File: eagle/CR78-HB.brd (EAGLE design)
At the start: 100 x 80 mm, 34 parts, among them Q1 2N3904, Q2 2N3904, Q3 2N3904, X1 22-23-2021

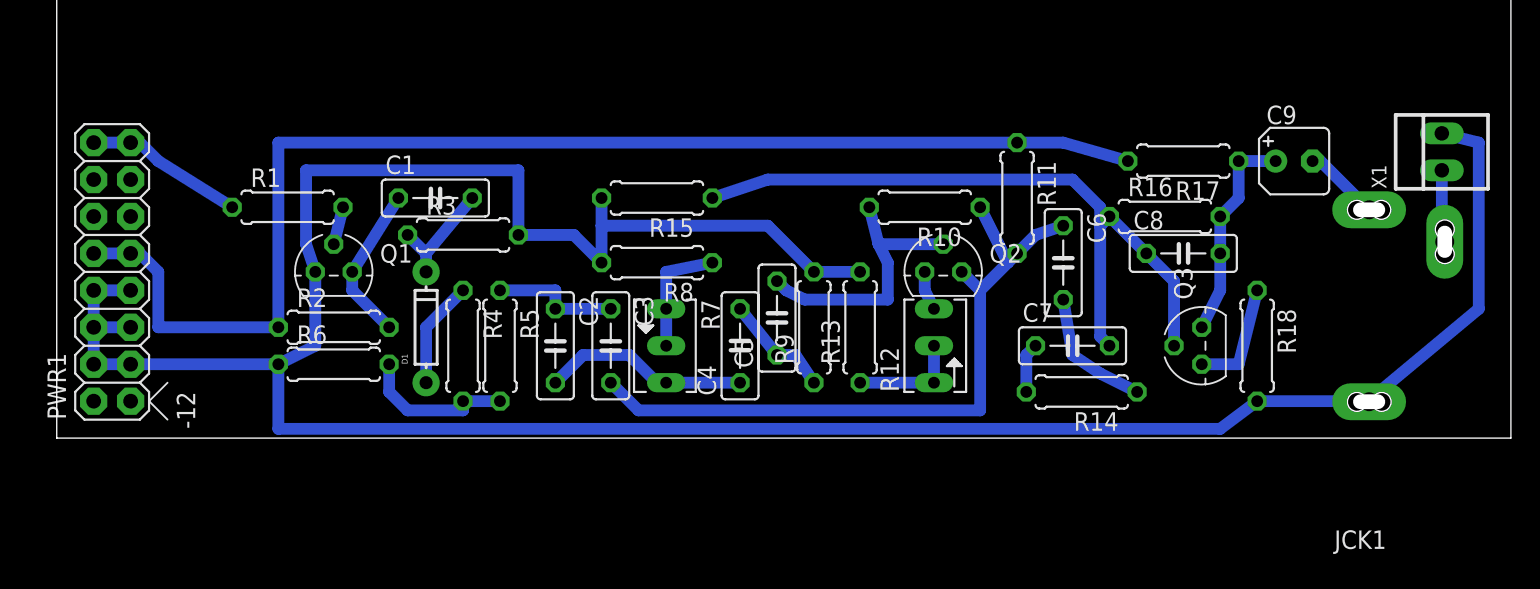
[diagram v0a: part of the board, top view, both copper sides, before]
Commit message: minimized routing
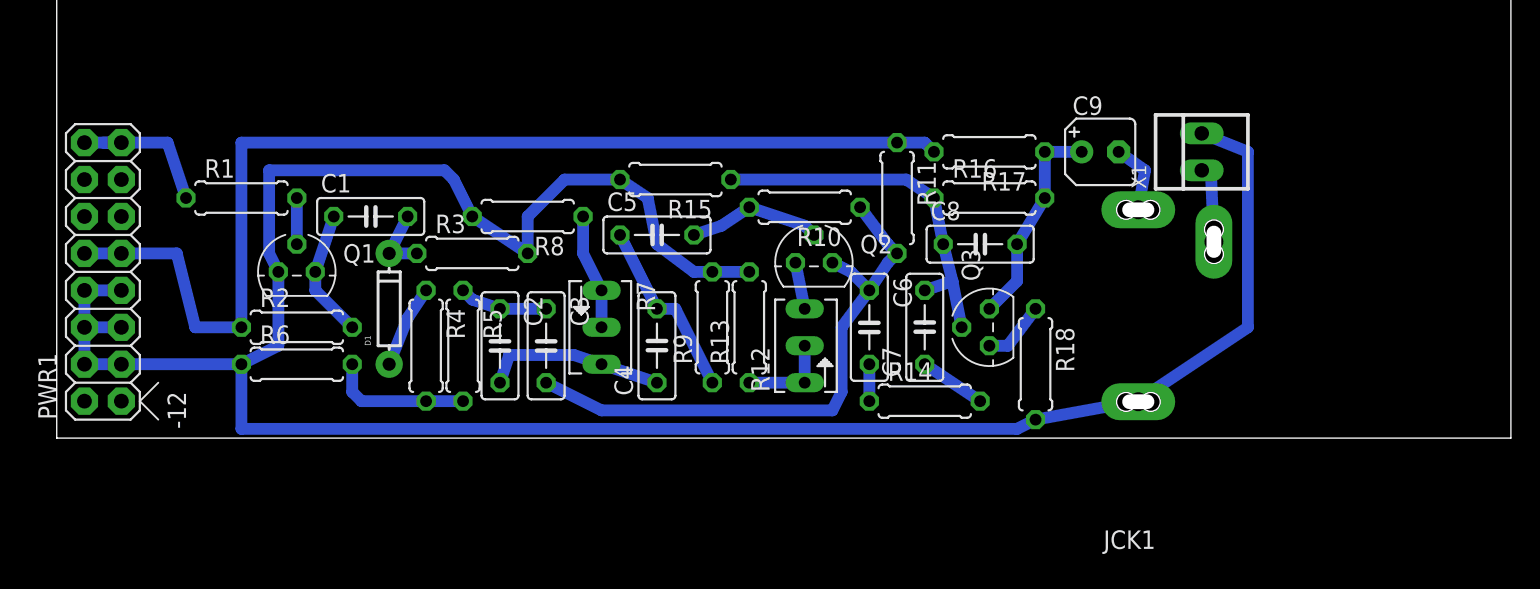
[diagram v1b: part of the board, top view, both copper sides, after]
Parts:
- moved X1 16.5 mm to (78.7, 19.7)
- moved JCK1 15.9 mm to (79.4, 0.00)
- moved R18 15.3 mm to (67.3, 5.08)
- moved Q3 14.7 mm to (64.1, 7.62)
- moved C6 14.1 mm to (55.9, 7.62)
- moved C8 14.0 mm to (63.5, 13.3)
- moved C9 13.4 mm to (71.8, 19.7)
- moved R17 13.4 mm to (64.1, 19.7)
- moved R16 12.1 mm to (64.1, 16.5)
- moved R14 10.8 mm to (59.7, 2.54), turned to 0 degrees
- moved C7 10.2 mm to (59.7, 7.62), turned to 90 degrees
- moved C5 10.0 mm to (41.3, 14.0), turned to 0 degrees
- moved R8 9.44 mm to (32.4, 15.2)
- moved Q2 8.91 mm to (52.1, 12.1)
- moved R12 8.89 mm to (51.4, 6.35)
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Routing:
- net N$18: track 49.1 -> 25.5 mm
- net GND: track 190.9 -> 169.8 mm
- net +12V: track 88.3 -> 75.3 mm
- net N$7: track 19.1 -> 9.21 mm
- net N$9: track 47.9 -> 39.7 mm
- net N$14: track 8.99 -> 2.54 mm
- net N$10: track 7.63 -> 12.6 mm
- net N$15: track 7.78 -> 4.44 mm
- net N$1: track 8.03 -> 4.74 mm
- net N$4: track 8.89 -> 6.08 mm
- net N$46: track 10.9 -> 8.88 mm
- net N$6: track 14.3 -> 12.5 mm
- net N$2: track 7.40 -> 5.71 mm
- net N$8: track 7.62 -> 6.35 mm
- net N$17: track 3.44 -> 4.58 mm
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
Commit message: cutout
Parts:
- moved R13 0.90 mm to (47.0, 8.26)
- moved C4 0.64 mm to (41.3, 6.99)
- moved R9 0.64 mm to (45.1, 8.26)
- moved C5 0.63 mm to (41.3, 14.6)
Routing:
- net GND: track 169.8 -> 168.9 mm
- net N$8: track 6.35 -> 7.03 mm
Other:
- board size 100 x 80 mm -> 100.6 x 80.6 mm
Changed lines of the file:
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@@
 <layer number="44" name="Drills" color="7" fill="1" visible="no" active="yes"/>
 <layer number="45" name="Holes" color="7" fill="1" visible="no" active="yes"/>
-<layer number="46" name="Milling" color="3" fill="1" visible="no" active="yes"/>
+<layer number="46" name="Milling" color="3" fill="1" visible="yes" active="yes"/>
 <layer number="47" name="Measures" color="7" fill="1" visible="no" active="yes"/>
 <layer number="48" name="Document" color="7" fill="1" visible="yes" active="yes"/>
@@
 <wire x1="100" y1="80" x2="0" y2="80" width="0" layer="20"/>
 <wire x1="0" y1="80" x2="0" y2="0" width="0" layer="20"/>
+<wire x1="-0.635" y1="-0.635" x2="-0.635" y2="21.59" width="1.6764" layer="46"/>
+<wire x1="-0.635" y1="21.59" x2="1.27" y2="22.86" width="1.6764" layer="46"/>
+<wire x1="1.27" y1="22.86" x2="81.915" y2="22.86" width="1.6764" layer="46"/>
+<wire x1="81.915" y1="22.86" x2="83.82" y2="21.59" width="1.6764" layer="46"/>
+<wire x1="83.82" y1="21.59" x2="83.82" y2="0" width="1.6764" layer="46"/>
+<wire x1="83.82" y1="0" x2="82.55" y2="-0.635" width="1.6764" layer="46"/>
+<wire x1="82.55" y1="-0.635" x2="-0.635" y2="-0.635" width="1.6764" layer="46"/>
 </plain>
 <attributes>
@@
 <element name="C2" library="rcl" package="C050-025X075" value="8n2" x="30.48" y="6.35" rot="R270"/>
 <element name="C3" library="rcl" package="C050-025X075" value="8n2" x="33.655" y="6.35" rot="R270"/>
-<element name="C4" library="rcl" package="C050-025X075" value="6n8" x="41.275" y="6.35" rot="R90"/>
-<element name="C5" library="rcl" package="C050-025X075" value="6n8" x="41.275" y="13.97"/>
+<element name="C4" library="rcl" package="C050-025X075" value="6n8" x="41.275" y="6.985" rot="R90"/>
+<element name="C5" library="rcl" package="C050-025X075" value="6n8" x="41.275" y="14.605"/>
 <element name="C6" library="rcl" package="C050-025X075" value="2n2" x="55.88" y="7.62" rot="R270"/>
 <element name="C7" library="rcl" package="C050-025X075" value="473" x="59.69" y="7.62" rot="R90"/>
@@
 <element name="R5" library="rcl" package="0207/7" value="15k" x="27.94" y="6.35" rot="R270"/>
 <element name="R8" library="rcl" package="0207/7" value="10k" x="32.385" y="15.24" rot="R180"/>
-<element name="R9" library="rcl" package="0207/7" value="15k" x="45.085" y="7.62" rot="R90"/>
-<element name="R13" library="rcl" package="0207/7" value="100R" x="47.625" y="7.62" rot="R90"/>
+<element name="R9" library="rcl" package="0207/7" value="15k" x="45.085" y="8.255" rot="R90"/>
+<element name="R13" library="rcl" package="0207/7" value="100R" x="46.99" y="8.255" rot="R90"/>
 <element name="R10" library="rcl" package="0207/7" value="1M5" x="51.435" y="15.875" rot="R180"/>
 <element name="R11" library="rcl" package="0207/7" value="10k" x="57.785" y="16.51" rot="R270"/>
@@
 <wire x1="1.905" y1="7.62" x2="1.905" y2="10.16" width="0.8128" layer="16"/>
 <wire x1="4.445" y1="5.08" x2="12.7" y2="5.08" width="0.8128" layer="16"/>
-<wire x1="47.625" y1="11.43" x2="45.085" y2="11.43" width="0.8128" layer="16"/>
+<wire x1="46.99" y1="12.065" x2="45.085" y2="12.065" width="0.8128" layer="16"/>
 <wire x1="14.605" y1="12.7" x2="15.24" y2="11.43" width="0.8128" layer="16"/>
 <wire x1="14.605" y1="18.415" x2="14.605" y2="12.7" width="0.8128" layer="16"/>
@@
 <wire x1="12.7" y1="0.635" x2="66.04" y2="0.635" width="0.8128" layer="16"/>
 <wire x1="12.7" y1="5.08" x2="12.7" y2="0.635" width="0.8128" layer="16"/>
-<wire x1="41.275" y1="13.335" x2="43.815" y2="11.43" width="0.8128" layer="16"/>
-<wire x1="43.815" y1="11.43" x2="45.085" y2="11.43" width="0.8128" layer="16"/>
+<wire x1="41.275" y1="13.335" x2="43.18" y2="12.065" width="0.8128" layer="16"/>
+<wire x1="43.18" y1="12.065" x2="45.085" y2="12.065" width="0.8128" layer="16"/>
 <wire x1="28.575" y1="15.24" x2="27.305" y2="17.78" width="0.8128" layer="16"/>
 <wire x1="27.305" y1="17.78" x2="26.67" y2="18.415" width="0.8128" layer="16"/>
@@
 <wire x1="35.56" y1="5.715" x2="31.115" y2="5.715" width="0.8128" layer="16"/>
 <wire x1="37.465" y1="5.08" x2="35.56" y2="5.715" width="0.8128" layer="16"/>
-<wire x1="37.465" y1="5.08" x2="41.275" y2="3.81" width="0.8128" layer="16"/>
+<wire x1="37.465" y1="5.08" x2="41.275" y2="4.445" width="0.8128" layer="16"/>
 </signal>
 <signal name="N$7">
@@
 <wire x1="47.625" y1="15.875" x2="51.435" y2="14.605" width="0.8128" layer="16"/>
 <wire x1="51.435" y1="14.605" x2="52.07" y2="13.97" width="0.8128" layer="16"/>
-<wire x1="43.815" y1="13.97" x2="45.72" y2="14.605" width="0.8128" layer="16"/>
+<wire x1="43.815" y1="14.605" x2="45.72" y2="14.605" width="0.8128" layer="16"/>
 <wire x1="45.72" y1="14.605" x2="47.625" y2="15.875" width="0.8128" layer="16"/>
 </signal>
@@
 <contactref element="R13" pad="1"/>
 <contactref element="R12" pad="S"/>
-<wire x1="51.435" y1="3.81" x2="47.625" y2="3.81" width="0.8128" layer="16"/>
+<wire x1="51.435" y1="3.81" x2="46.99" y2="4.445" width="0.8128" layer="16"/>
 <wire x1="51.435" y1="3.81" x2="51.435" y2="6.35" width="0.8128" layer="16"/>
 </signal>
@@
 <contactref element="C4" pad="2"/>
 <contactref element="R9" pad="1"/>
-<wire x1="38.735" y1="13.97" x2="41.275" y2="8.89" width="0.8128" layer="16"/>
-<wire x1="41.275" y1="8.89" x2="42.545" y2="8.89" width="0.8128" layer="16"/>
-<wire x1="42.545" y1="8.89" x2="45.085" y2="3.81" width="0.8128" layer="16"/>
+<wire x1="38.735" y1="14.605" x2="41.275" y2="9.525" width="0.8128" layer="16"/>
+<wire x1="41.275" y1="9.525" x2="42.545" y2="8.89" width="0.8128" layer="16"/>
+<wire x1="42.545" y1="8.89" x2="45.085" y2="4.445" width="0.8128" layer="16"/>
 </signal>
 <signal name="N$11">

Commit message: gcode
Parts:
- moved R9 0.63 mm to (44.5, 8.26)
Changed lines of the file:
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@@
 <?xml version="1.0" encoding="utf-8"?>
 <!DOCTYPE eagle SYSTEM "eagle.dtd">
-<eagle version="7.2.0">
+<eagle version="7.1.0">
 <drawing>
 <settings>
@@
 <wire x1="83.82" y1="0" x2="82.55" y2="-0.635" width="1.6764" layer="46"/>
 <wire x1="82.55" y1="-0.635" x2="-0.635" y2="-0.635" width="1.6764" layer="46"/>
+<rectangle x1="1.27" y1="5.08" x2="5.08" y2="10.16" layer="16"/>
 </plain>
 <attributes>
@@
 <element name="R5" library="rcl" package="0207/7" value="15k" x="27.94" y="6.35" rot="R270"/>
 <element name="R8" library="rcl" package="0207/7" value="10k" x="32.385" y="15.24" rot="R180"/>
-<element name="R9" library="rcl" package="0207/7" value="15k" x="45.085" y="8.255" rot="R90"/>
+<element name="R9" library="rcl" package="0207/7" value="15k" x="44.45" y="8.255" rot="R90"/>
 <element name="R13" library="rcl" package="0207/7" value="100R" x="46.99" y="8.255" rot="R90"/>
 <element name="R10" library="rcl" package="0207/7" value="1M5" x="51.435" y="15.875" rot="R180"/>
@@
 <wire x1="1.905" y1="7.62" x2="1.905" y2="10.16" width="0.8128" layer="16"/>
 <wire x1="4.445" y1="5.08" x2="12.7" y2="5.08" width="0.8128" layer="16"/>
-<wire x1="46.99" y1="12.065" x2="45.085" y2="12.065" width="0.8128" layer="16"/>
+<wire x1="46.99" y1="12.065" x2="44.45" y2="12.065" width="0.8128" layer="16"/>
 <wire x1="14.605" y1="12.7" x2="15.24" y2="11.43" width="0.8128" layer="16"/>
 <wire x1="14.605" y1="18.415" x2="14.605" y2="12.7" width="0.8128" layer="16"/>
@@
 <wire x1="12.7" y1="5.08" x2="12.7" y2="0.635" width="0.8128" layer="16"/>
 <wire x1="41.275" y1="13.335" x2="43.18" y2="12.065" width="0.8128" layer="16"/>
-<wire x1="43.18" y1="12.065" x2="45.085" y2="12.065" width="0.8128" layer="16"/>
+<wire x1="43.18" y1="12.065" x2="44.45" y2="12.065" width="0.8128" layer="16"/>
 <wire x1="28.575" y1="15.24" x2="27.305" y2="17.78" width="0.8128" layer="16"/>
 <wire x1="27.305" y1="17.78" x2="26.67" y2="18.415" width="0.8128" layer="16"/>
@@
 <wire x1="38.735" y1="14.605" x2="41.275" y2="9.525" width="0.8128" layer="16"/>
 <wire x1="41.275" y1="9.525" x2="42.545" y2="8.89" width="0.8128" layer="16"/>
-<wire x1="42.545" y1="8.89" x2="45.085" y2="4.445" width="0.8128" layer="16"/>
+<wire x1="42.545" y1="8.89" x2="44.45" y2="4.445" width="0.8128" layer="16"/>
 </signal>
 <signal name="N$11">

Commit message: lb
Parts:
- C2: value 8n2 -> 12n
- C3: value 8n2 -> 18n
- C4: value 6n8 -> 12n
- C5: value 6n8 -> 10n
- C6: value 2n2 -> 8n2
- R14: value 1M5 -> 680k
- moved R9 0.63 mm to (45.1, 8.26)
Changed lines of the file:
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@@
 <?xml version="1.0" encoding="utf-8"?>
 <!DOCTYPE eagle SYSTEM "eagle.dtd">
-<eagle version="7.1.0">
+<eagle version="7.2.0">
 <drawing>
 <settings>
@@
 <wire x1="83.82" y1="0" x2="82.55" y2="-0.635" width="1.6764" layer="46"/>
 <wire x1="82.55" y1="-0.635" x2="-0.635" y2="-0.635" width="1.6764" layer="46"/>
-<rectangle x1="1.27" y1="5.08" x2="5.08" y2="10.16" layer="16"/>
 </plain>
 <attributes>
@@
 <elements>
 <element name="C1" library="rcl" package="C050-025X075" value="27n" x="21.59" y="15.24"/>
-<element name="C2" library="rcl" package="C050-025X075" value="8n2" x="30.48" y="6.35" rot="R270"/>
-<element name="C3" library="rcl" package="C050-025X075" value="8n2" x="33.655" y="6.35" rot="R270"/>
-<element name="C4" library="rcl" package="C050-025X075" value="6n8" x="41.275" y="6.985" rot="R90"/>
-<element name="C5" library="rcl" package="C050-025X075" value="6n8" x="41.275" y="14.605"/>
-<element name="C6" library="rcl" package="C050-025X075" value="2n2" x="55.88" y="7.62" rot="R270"/>
+<element name="C2" library="rcl" package="C050-025X075" value="12n" x="30.48" y="6.35" rot="R270"/>
+<element name="C3" library="rcl" package="C050-025X075" value="18n" x="33.655" y="6.35" rot="R270"/>
+<element name="C4" library="rcl" package="C050-025X075" value="12n" x="41.275" y="6.985" rot="R90"/>
+<element name="C5" library="rcl" package="C050-025X075" value="10n" x="41.275" y="14.605"/>
+<element name="C6" library="rcl" package="C050-025X075" value="8n2" x="55.88" y="7.62" rot="R270"/>
 <element name="C7" library="rcl" package="C050-025X075" value="473" x="59.69" y="7.62" rot="R90"/>
 <element name="C8" library="rcl" package="C050-025X075" value="47p" x="63.5" y="13.335"/>
@@
 <element name="Q3" library="808_lt" package="TO92" value="2N3904" x="64.135" y="7.62" rot="R90"/>
 <element name="R3" library="rcl" package="0207/7" value="270k" x="28.575" y="12.7"/>
-<element name="R14" library="rcl" package="0207/7" value="1M5" x="59.69" y="2.54"/>
+<element name="R14" library="rcl" package="0207/7" value="680k" x="59.69" y="2.54"/>
 <element name="R16" library="rcl" package="0207/7" value="470k" x="64.135" y="16.51"/>
 <element name="R17" library="rcl" package="0207/7" value="47k" x="64.135" y="19.685" rot="R180"/>
@@
 <element name="R5" library="rcl" package="0207/7" value="15k" x="27.94" y="6.35" rot="R270"/>
 <element name="R8" library="rcl" package="0207/7" value="10k" x="32.385" y="15.24" rot="R180"/>
-<element name="R9" library="rcl" package="0207/7" value="15k" x="44.45" y="8.255" rot="R90"/>
+<element name="R9" library="rcl" package="0207/7" value="15k" x="45.085" y="8.255" rot="R90"/>
 <element name="R13" library="rcl" package="0207/7" value="100R" x="46.99" y="8.255" rot="R90"/>
 <element name="R10" library="rcl" package="0207/7" value="1M5" x="51.435" y="15.875" rot="R180"/>
@@
 <wire x1="1.905" y1="7.62" x2="1.905" y2="10.16" width="0.8128" layer="16"/>
 <wire x1="4.445" y1="5.08" x2="12.7" y2="5.08" width="0.8128" layer="16"/>
-<wire x1="46.99" y1="12.065" x2="44.45" y2="12.065" width="0.8128" layer="16"/>
+<wire x1="46.99" y1="12.065" x2="45.085" y2="12.065" width="0.8128" layer="16"/>
 <wire x1="14.605" y1="12.7" x2="15.24" y2="11.43" width="0.8128" layer="16"/>
 <wire x1="14.605" y1="18.415" x2="14.605" y2="12.7" width="0.8128" layer="16"/>
@@
 <wire x1="12.7" y1="5.08" x2="12.7" y2="0.635" width="0.8128" layer="16"/>
 <wire x1="41.275" y1="13.335" x2="43.18" y2="12.065" width="0.8128" layer="16"/>
-<wire x1="43.18" y1="12.065" x2="44.45" y2="12.065" width="0.8128" layer="16"/>
+<wire x1="43.18" y1="12.065" x2="45.085" y2="12.065" width="0.8128" layer="16"/>
 <wire x1="28.575" y1="15.24" x2="27.305" y2="17.78" width="0.8128" layer="16"/>
 <wire x1="27.305" y1="17.78" x2="26.67" y2="18.415" width="0.8128" layer="16"/>
@@
 <wire x1="38.735" y1="14.605" x2="41.275" y2="9.525" width="0.8128" layer="16"/>
 <wire x1="41.275" y1="9.525" x2="42.545" y2="8.89" width="0.8128" layer="16"/>
-<wire x1="42.545" y1="8.89" x2="44.45" y2="4.445" width="0.8128" layer="16"/>
+<wire x1="42.545" y1="8.89" x2="45.085" y2="4.445" width="0.8128" layer="16"/>
 </signal>
 <signal name="N$11">

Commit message: lc
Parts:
- C2, C4: value 12n -> 22n
- C3: value 18n -> 27n
- C5: value 10n -> 22n
- C6: value 8n2 -> 10n
- R14: value 680k -> 560k
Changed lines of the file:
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@@
 <elements>
 <element name="C1" library="rcl" package="C050-025X075" value="27n" x="21.59" y="15.24"/>
-<element name="C2" library="rcl" package="C050-025X075" value="12n" x="30.48" y="6.35" rot="R270"/>
-<element name="C3" library="rcl" package="C050-025X075" value="18n" x="33.655" y="6.35" rot="R270"/>
-<element name="C4" library="rcl" package="C050-025X075" value="12n" x="41.275" y="6.985" rot="R90"/>
-<element name="C5" library="rcl" package="C050-025X075" value="10n" x="41.275" y="14.605"/>
-<element name="C6" library="rcl" package="C050-025X075" value="8n2" x="55.88" y="7.62" rot="R270"/>
+<element name="C2" library="rcl" package="C050-025X075" value="22n" x="30.48" y="6.35" rot="R270"/>
+<element name="C3" library="rcl" package="C050-025X075" value="27n" x="33.655" y="6.35" rot="R270"/>
+<element name="C4" library="rcl" package="C050-025X075" value="22n" x="41.275" y="6.985" rot="R90"/>
+<element name="C5" library="rcl" package="C050-025X075" value="22n" x="41.275" y="14.605"/>
+<element name="C6" library="rcl" package="C050-025X075" value="10n" x="55.88" y="7.62" rot="R270"/>
 <element name="C7" library="rcl" package="C050-025X075" value="473" x="59.69" y="7.62" rot="R90"/>
 <element name="C8" library="rcl" package="C050-025X075" value="47p" x="63.5" y="13.335"/>
@@
 <element name="Q3" library="808_lt" package="TO92" value="2N3904" x="64.135" y="7.62" rot="R90"/>
 <element name="R3" library="rcl" package="0207/7" value="270k" x="28.575" y="12.7"/>
-<element name="R14" library="rcl" package="0207/7" value="680k" x="59.69" y="2.54"/>
+<element name="R14" library="rcl" package="0207/7" value="560k" x="59.69" y="2.54"/>
 <element name="R16" library="rcl" package="0207/7" value="470k" x="64.135" y="16.51"/>
 <element name="R17" library="rcl" package="0207/7" value="47k" x="64.135" y="19.685" rot="R180"/>
